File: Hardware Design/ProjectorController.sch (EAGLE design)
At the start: 18 parts, among them J1 5747844-4, J2 Cap Buttons, J3 Prog, J4 Prog/Run, J5 10118194-0001LF, U1 ESP-WROOM-32, U2 SP3232EEN-L

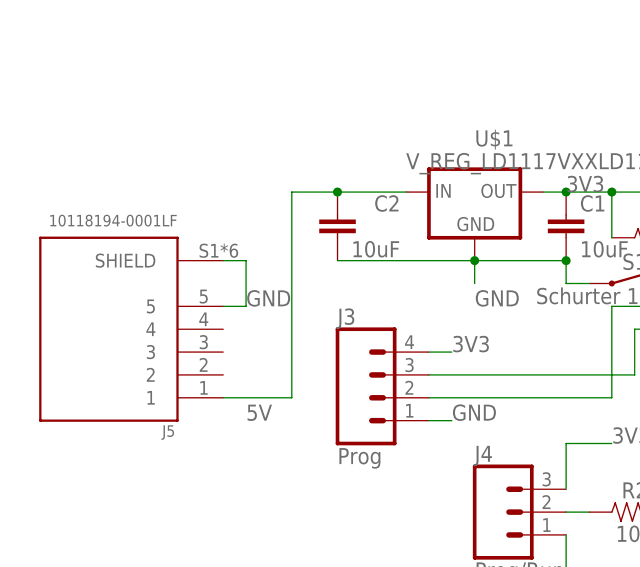
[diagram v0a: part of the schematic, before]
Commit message: Revert "ED-33 Major board redesign to make smaller"
This reverts commit ff5836e82a7b4c6ccf7f1796d2610aee96480eab.
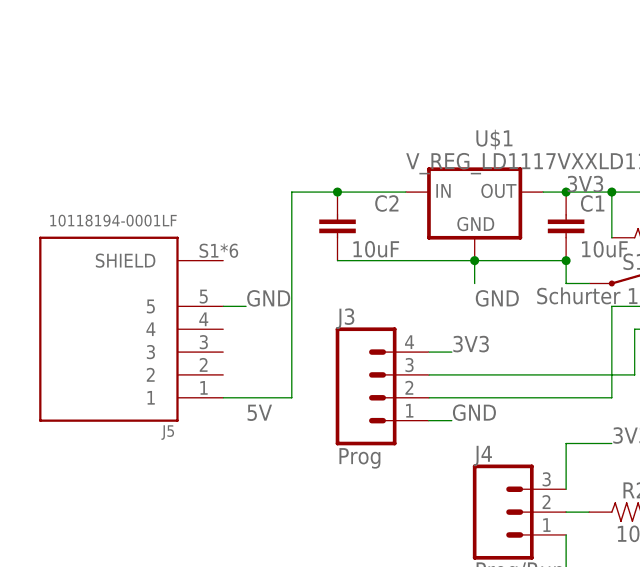
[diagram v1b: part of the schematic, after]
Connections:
- net GND: no longer J5.SHIELD
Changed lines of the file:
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@@
 <?xml version="1.0" encoding="utf-8"?>
 <!DOCTYPE eagle SYSTEM "eagle.dtd">
-<eagle version="9.6.1">
+<eagle version="9.5.2">
 <drawing>
 <settings>
@@
 <wire x1="-88.9" y1="38.1" x2="-86.36" y2="38.1" width="0.1524" layer="91"/>
 <label x="-86.36" y="38.1" size="1.778" layer="95"/>
-<pinref part="J5" gate="G$1" pin="SHIELD"/>
-<wire x1="-88.9" y1="43.18" x2="-86.36" y2="43.18" width="0.1524" layer="91"/>
-<wire x1="-86.36" y1="43.18" x2="-86.36" y2="38.1" width="0.1524" layer="91"/>
-</segment>
-<segment>
+</segment>
+<segment>
